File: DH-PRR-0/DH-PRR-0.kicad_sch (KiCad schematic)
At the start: 6 parts, among them U1 Si4735-D60-GU

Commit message: mcu, memory receptacle, initial power topo
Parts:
- removed C1: C, symbol Device:C
- removed L1: L_Ferrite, symbol Device:L_Ferrite
- removed R1, R2, R3: R, symbol Device:R
- removed U1: Si4735-D60-GU, Package_SO:SSOP-24_3.9x8.7mm_P0.635mm, symbol RF_AM_FM:Si4735-D60-GU
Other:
- added sheet AM-FM RECEIVER (rf_ic.kicad_sch)
- added sheet MEMORY (memory.kicad_sch)
- added sheet MICROCONTROLLER UNIT (microcontroller.kicad_sch)
- added sheet POWER MANAGEMENT (power_mgmt.kicad_sch)
- added sheet USB-C (usb_c_receptacle.kicad_sch)

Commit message: i dont remember
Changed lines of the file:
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@@
 	(sheet
 		(at 60.96 25.4)
-		(size 29.21 38.1)
+		(size 29.21 76.2)
 		(exclude_from_sim no)
 		(in_bom yes)
@@
 		)
 		(property "Sheetfile" "microcontroller.kicad_sch"
-			(at 60.96 64.0846 0)
+			(at 60.96 102.1846 0)
 			(show_name no)
 			(do_not_autoplace no)
@@
 	)
 	(sheet
-		(at 25.4 25.4)
-		(size 31.75 38.1)
+		(at 93.98 68.58)
+		(size 31.75 33.02)
 		(exclude_from_sim no)
 		(in_bom yes)
@@
 		)
 		(property "Sheetname" "MEMORY"
-			(at 25.4 24.6884 0)
+			(at 93.98 67.8684 0)
 			(show_name no)
 			(do_not_autoplace no)
@@
 		)
 		(property "Sheetfile" "memory.kicad_sch"
-			(at 25.4 64.0846 0)
+			(at 93.98 102.1846 0)
 			(show_name no)
 			(do_not_autoplace no)
@@
 	)
 	(sheet
-		(at 93.98 25.4)
+		(at 31.75 81.28)
 		(size 25.4 20.32)
 		(exclude_from_sim no)
@@
 		)
 		(property "Sheetname" "AM-FM RECEIVER"
-			(at 93.98 24.6884 0)
+			(at 31.75 80.5684 0)
 			(show_name no)
 			(do_not_autoplace no)
@@
 		)
 		(property "Sheetfile" "rf_ic.kicad_sch"
-			(at 93.98 46.3046 0)
+			(at 31.75 102.1846 0)
 			(show_name no)
 			(do_not_autoplace no)
@@
 		)
 		(pin "DFS" input
-			(at 119.38 35.56 0)
+			(at 57.15 91.44 0)
 			(effects
 				(font
@@
 		)
 		(pin "DOUT" output
-			(at 119.38 27.94 0)
+			(at 57.15 83.82 0)
 			(effects
 				(font
@@
 		)
 		(pin "GPO1" output
-			(at 93.98 40.64 180)
+			(at 31.75 96.52 180)
 			(effects
 				(font
@@
 		)
 		(pin "GPO2/[~{INT}]" output
-			(at 93.98 43.18 180)
+			(at 31.75 99.06 180)
 			(effects
 				(font
@@
 		)
 		(pin "LOUT/[DFS]" bidirectional
-			(at 119.38 33.02 0)
+			(at 57.15 88.9 0)
 			(effects
 				(font
@@
 		)
 		(pin "ROUT/[DOUT]" output
-			(at 119.38 30.48 0)
+			(at 57.15 86.36 0)
 			(effects
 				(font
@@
 		)
 		(pin "SCLK" input
-			(at 93.98 35.56 180)
+			(at 31.75 91.44 180)
 			(effects
 				(font
@@
 		)
 		(pin "SDIO" bidirectional
-			(at 93.98 33.02 180)
+			(at 31.75 88.9 180)
 			(effects
 				(font
@@
 		)
 		(pin "~{RST}" input
-			(at 93.98 27.94 180)
+			(at 31.75 83.82 180)
 			(effects
 				(font
@@
 		)
 		(pin "~{SEN}" input
-			(at 93.98 30.48 180)
+			(at 31.75 86.36 180)
 			(effects
 				(font
@@
 	)
 	(sheet
-		(at 93.98 50.8)
-		(size 25.4 12.7)
+		(at 31.75 25.4)
+		(size 25.4 50.8)
 		(exclude_from_sim no)
 		(in_bom yes)
@@
 		)
 		(property "Sheetname" "POWER MANAGEMENT"
-			(at 93.98 50.0884 0)
+			(at 31.75 24.6884 0)
 			(show_name no)
 			(do_not_autoplace no)
@@
 		)
 		(property "Sheetfile" "power_mgmt.kicad_sch"
-			(at 93.98 64.0846 0)
+			(at 31.75 76.7846 0)
 			(show_name no)
 			(do_not_autoplace no)
@@
 	)
 	(sheet
-		(at 123.19 25.4)
+		(at 93.98 25.4)
 		(size 31.75 38.1)
 		(exclude_from_sim no)
@@
 		)
 		(property "Sheetname" "USB-C"
-			(at 123.19 24.6884 0)
+			(at 93.98 24.6884 0)
 			(show_name no)
 			(do_not_autoplace no)
@@
 		)
 		(property "Sheetfile" "usb_c_receptacle.kicad_sch"
-			(at 123.19 64.0846 0)
-			(show_name no)
-			(do_not_autoplace no)
+			(at 93.98 64.0846 0)
+			(show_name no)
+			(do_not_autoplace no)

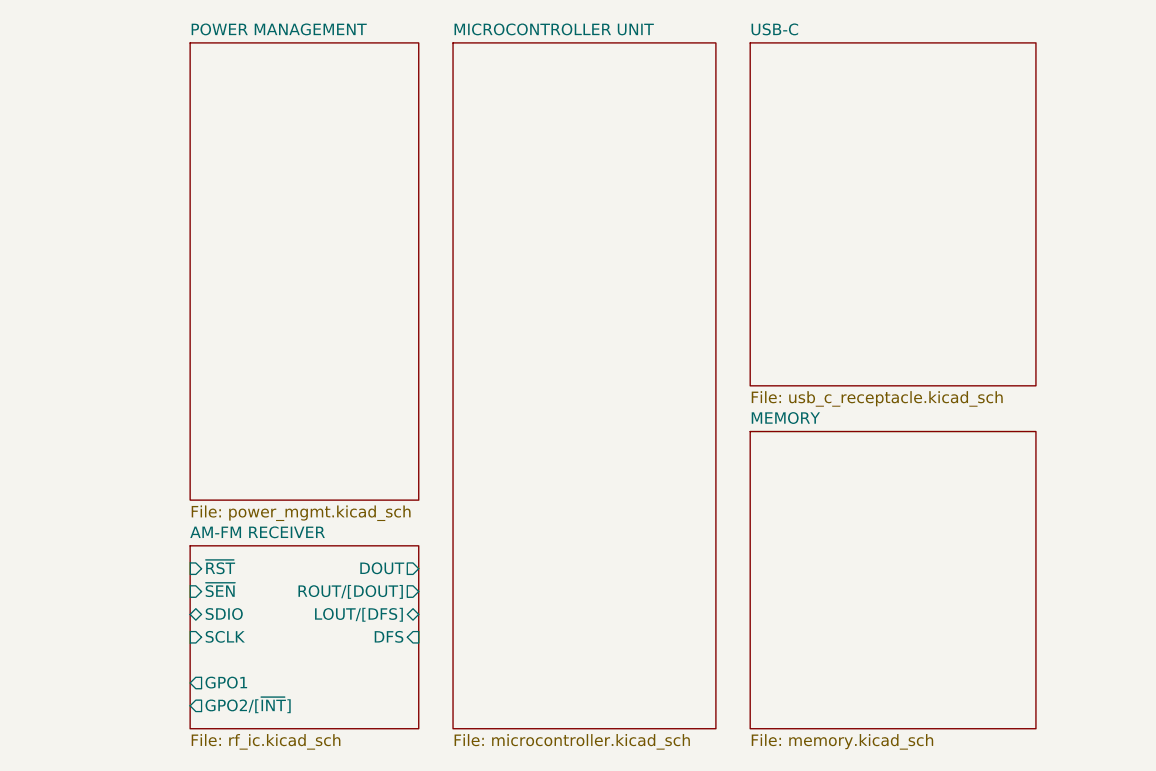
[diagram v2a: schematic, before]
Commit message: changed usb-spi bridge to host bridge, now functional
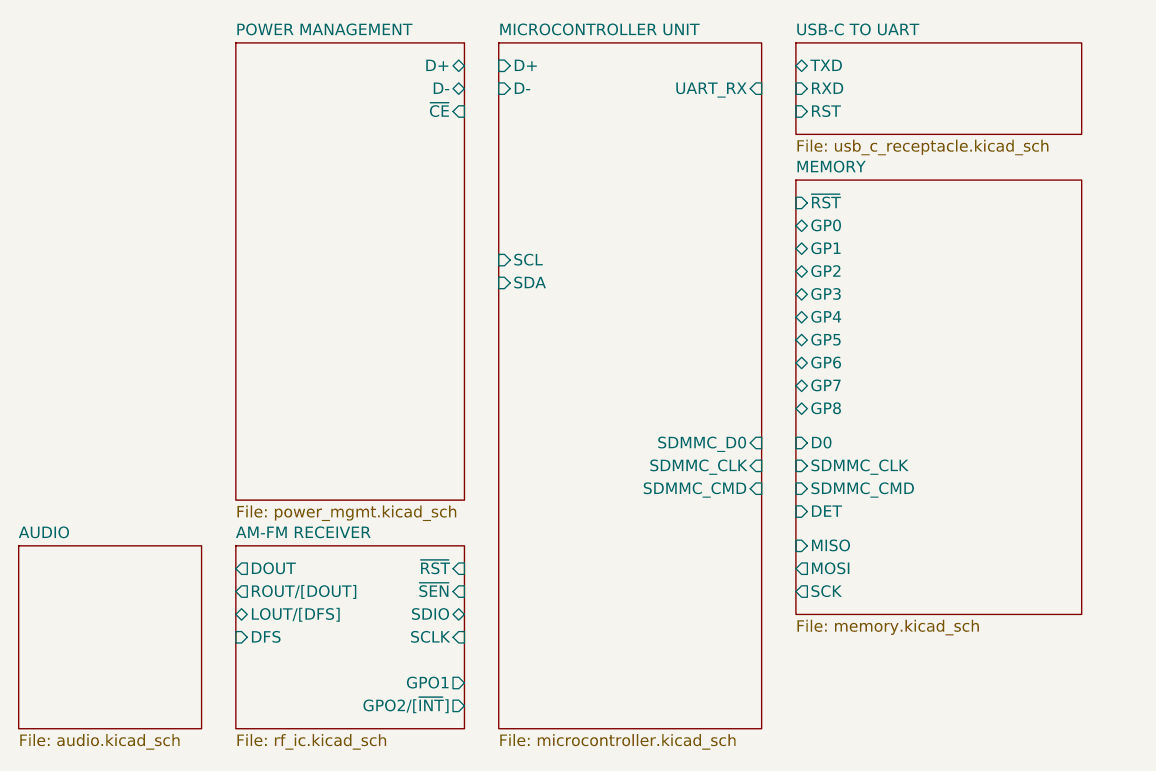
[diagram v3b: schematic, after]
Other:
- sheet USB-C renamed USB-C TO UART
- added sheet AUDIO (audio.kicad_sch)
- sheet MEMORY ports: added D0, DET, GP0, GP1, GP2, GP3, GP4, GP5, GP6, GP7, GP8, MISO, MOSI, SCK, SDMMC_CLK, SDMMC_CMD, ~{RST}; removed none
- sheet MICROCONTROLLER UNIT ports: added D+, D-, SCL, SDA, SDMMC_CLK, SDMMC_CMD, SDMMC_D0, UART_RX; removed none
- sheet POWER MANAGEMENT ports: added D+, D-, ~{CE}; removed none
- sheet USB-C TO UART ports: added RST, RXD, TXD; removed none
